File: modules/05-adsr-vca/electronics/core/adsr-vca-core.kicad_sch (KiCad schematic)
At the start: 8 parts, among them J2 Conn_02x03_Odd_Even, J3 Conn_02x03_Odd_Even, J4 Conn_02x06_Odd_Even, J8 Conn_02x03_Odd_Even

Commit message: ADSR+VCA JLCPCB verified for v1.0
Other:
- company: (none) -> Shmøergh
- title: (none) -> ADSR + VCA
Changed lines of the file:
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@@
 	(generator_version "9.0")
 	(paper "A4")
+	(title_block
+		(title "ADSR + VCA")
+		(date "2025-12-11")
+		(company "Shmøergh")
+	)
 	(text "Power"
 		(exclude_from_sim no)

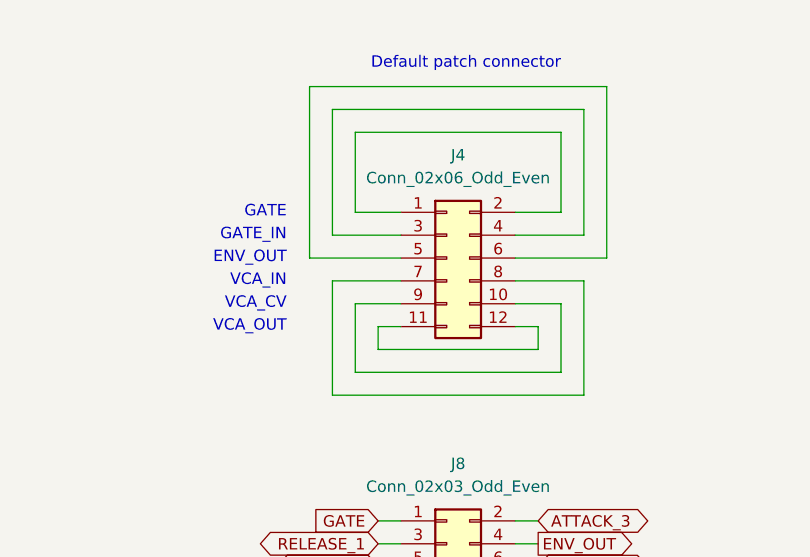
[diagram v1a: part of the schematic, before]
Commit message: Fixed ADSR default connector
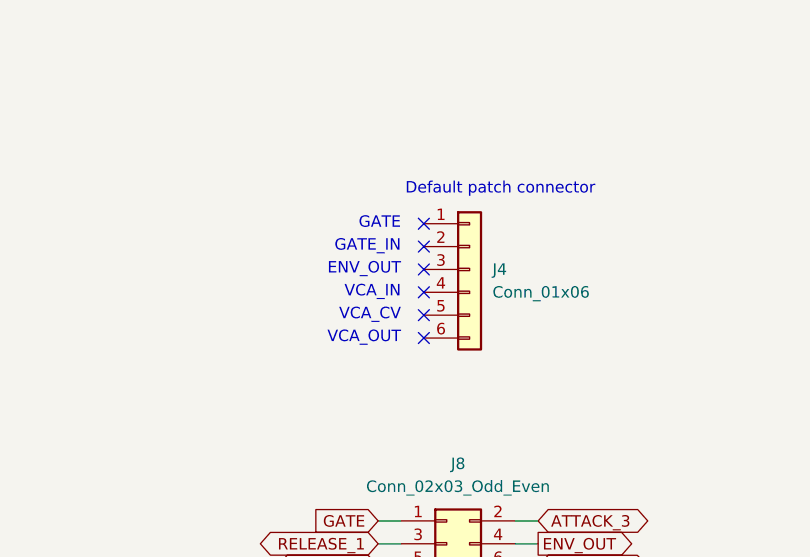
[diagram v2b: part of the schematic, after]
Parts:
- removed J4: Conn_02x06_Odd_Even, Connector_PinHeader_2.54mm:PinHeader_2x06_P2.54mm_Vertical, symbol Connector_Generic:Conn_02x06_Odd_Even
- added J4: Conn_01x06, Connector_PinSocket_2.54mm:PinSocket_1x06_P2.54mm_Vertical, symbol Connector_Generic:Conn_01x06
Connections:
- no-connect marks 0 -> 6

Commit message: Finished BOM for ADSR
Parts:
- J2, J3, J8: CHECKED (none) -> YES; Mouser Part no. (none) -> 200-TSW10307TD; Part URL (none) -> https://mou.sr/4liCQlU
- J4: CHECKED (none) -> YES; Mouser Part no. (none) -> 200-SSW10601TMS; Part URL https://mou.sr/4lnf48h -> https://mou.sr/4puxA0F
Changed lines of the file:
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@@
 			)
 		)
-		(property "Part URL" ""
+		(property "Part URL" "https://mou.sr/4liCQlU"
 			(at 213.36 114.3 0)
 			(effects
@@
 		)
 		(property "LCSC" ""
+			(at 213.36 114.3 0)
+			(effects
+				(font
+					(size 1.27 1.27)
+				)
+				(hide yes)
+			)
+		)
+		(property "CHECKED" "YES"
+			(at 213.36 114.3 0)
+			(effects
+				(font
+					(size 1.27 1.27)
+				)
+				(hide yes)
+			)
+		)
+		(property "Mouser Part no." "200-TSW10307TD"
 			(at 213.36 114.3 0)
 			(effects
@@
 			)
 		)
-		(property "Part URL" "https://mou.sr/4lnf48h"
+		(property "Part URL" "https://mou.sr/4puxA0F"
 			(at 215.9 40.64 0)
 			(effects
@@
 		)
 		(property "Part no." "200-SSW10601TS"
+			(at 215.9 40.64 0)
+			(effects
+				(font
+					(size 1.27 1.27)
+				)
+				(hide yes)
+			)
+		)
+		(property "CHECKED" "YES"
+			(at 215.9 40.64 0)
+			(effects
+				(font
+					(size 1.27 1.27)
+				)
+				(hide yes)
+			)
+		)
+		(property "Mouser Part no." "200-SSW10601TMS"
 			(at 215.9 40.64 0)
 			(effects
@@
 			)
 		)
-		(property "Part URL" ""
+		(property "Part URL" "https://mou.sr/4liCQlU"
 			(at 213.36 92.71 0)
 			(effects
@@
 		)
 		(property "LCSC" ""
+			(at 213.36 92.71 0)
+			(effects
+				(font
+					(size 1.27 1.27)
+				)
+				(hide yes)
+			)
+		)
+		(property "CHECKED" "YES"
+			(at 213.36 92.71 0)
+			(effects
+				(font
+					(size 1.27 1.27)
+				)
+				(hide yes)
+			)
+		)
+		(property "Mouser Part no." "200-TSW10307TD"
 			(at 213.36 92.71 0)
 			(effects
@@
 			)
 		)
-		(property "Part URL" ""
+		(property "Part URL" "https://mou.sr/4liCQlU"
 			(at 213.36 71.12 0)
 			(effects
@@
 			(at 213.36 71.12 0)
 			(effects
+				(font
+					(size 1.27 1.27)
+				)
+				(hide yes)
+			)
+		)
+		(property "CHECKED" "YES"
+			(at 213.36 71.12 0)
+			(effects
+				(font
+					(size 1.27 1.27)
+				)
+				(hide yes)
+			)
+		)
+		(property "Mouser Part no." "200-TSW10307TD"
+			(at 213.36 71.12 0)
+			(effects

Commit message: Set ADSR core default patch connector to DNP
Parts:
- J4: now not fitted
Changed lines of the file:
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@@
 		(in_bom yes)
 		(on_board yes)
-		(dnp no)
+		(dnp yes)
 		(fields_autoplaced yes)
 		(property "Reference" "J4"
@@
 			(at 215.9 40.64 0)
 			(effects
+				(font
+					(size 1.27 1.27)
+				)
+				(hide yes)
+			)
+		)
+		(property "Part No." ""
+			(at 215.9 40.64 0)
+			(effects
